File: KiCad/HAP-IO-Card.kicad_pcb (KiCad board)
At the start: 2 copper layers, 110 x 72 mm, 229 parts, among them CON601 AVR-JTAG-10, J201 TE_Connectivity_1-282834-0, J202 TE_Connectivity_282834-6, J203 GS3, J204 GS3, J205 GS3, J206 GS3, J207 GS3, J208 GS3, J209 GS3, J210 GS3, J211 TE_Connectivity_282834-6, J212 TE_Connectivity_1-282834-0, J401 TE_Connectivity_1-282834-0, J402 TE_Connectivity_282834-6, J501 TE_Connectivity_282834-3, J502 CONN_01X03_FEMALE, J601 ISP0, J602 ISP1, J603 CONN_01X02, J604 CONN_01X02, J605 CONN_01X02, J606 CONN_01X02, J607 CONN_01X03, J608 CONN_01X03, J701 5V_I/O_2, J702 5V_I/O_1, J703 NEO1, J704 NEO2, J705 NEO3, J706 NEO4, J707 CONN_01X03, Q201 ZXTN25050DFHTA, Q202 ZXTN25050DFHTA, Q203 ZXTN25050DFHTA, Q204 ZXTN25050DFHTA, Q205 ZXTN25050DFHTA, Q206 ZXTN25050DFHTA, Q207 ZXTN25050DFHTA, Q208 ZXTN25050DFHTA, U201 LTV-354T, U202 LTV-354T, U203 LTV-354T, U204 LTV-354T, U205 LTV-354T, U206 LTV-354T, U207 LTV-354T, U208 LTV-354T, U209 MCP23017, U401 ADS1115IDGST, U402 ADS1115IDGST, U501 LM1086-5V, U502 LM1086-3.3V, U701 TXB0102DCT

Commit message: More routing
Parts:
- CON601: footprint Pin_Headers:Pin_Header_Straight_2x06_Pitch2.54mm -> Pin_Headers:Pin_Header_Straight_2x05_Pitch2.54mm
- moved C409 6.62 mm to (118.2, 58.4), turned to 180 degrees
- moved U402 3.28 mm to (118.0, 52.7), turned to 90 degrees
- moved J203 2.16 mm to (128.3, 25.9)
- moved J204 2.16 mm to (124.7, 25.9)
- moved J205 2.16 mm to (121.1, 25.9)
- moved J206 2.16 mm to (117.4, 25.9)
- moved J207 2.16 mm to (113.5, 25.9)
- moved J208 2.16 mm to (109.9, 25.9)
- moved J209 2.16 mm to (106.3, 25.9)
- moved J210 2.16 mm to (102.7, 25.9)
- moved C506 1.20 mm to (66.8, 80.2)
- moved J601 1.11 mm to (60.8, 75.5)
- moved J602 1.11 mm to (56.7, 75.5)
- moved Q203 0.80 mm to (105.0, 37.9)
- moved C702 0.64 mm to (108.0, 59.6)
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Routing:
- net POWER3V3: track 73.6 -> 474.9 mm, vias 4 -> 12
- net SENSE_RDY_1: track 0.00 -> 116.0 mm
- net SENSE_SCL: track 0.00 -> 91.9 mm, vias 0 -> 2
- net DI7: track 0.00 -> 90.7 mm, vias 0 -> 4
- net DI8: track 0.00 -> 90.6 mm, vias 0 -> 5
- net 5V_I/O_1: track 6.31 -> 95.7 mm, vias 0 -> 6
- net SENSE_SDA: track 0.00 -> 88.5 mm, vias 0 -> 3
- net DI5: track 0.00 -> 85.6 mm, vias 0 -> 3
- net SENSE_RDY_2: track 0.00 -> 83.0 mm, vias 0 -> 7
- net 5V_I/O_Enable: track 0.00 -> 81.1 mm, vias 0 -> 4
- net DI6: track 0.00 -> 78.3 mm, vias 0 -> 5
- net POWER5V: track 283.7 -> 360.5 mm, vias 2 -> 8
- net Net-(JP302-Pad2): track 0.00 -> 76.1 mm
- net +12V: track 24.2 -> 97.9 mm
- net DI2: track 0.00 -> 73.2 mm, vias 0 -> 7
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- added copper zone on B.Cu, net Earth
- added copper zone on F.Cu, net Earth
- added copper zone on F.Cu, net POWER3V3
- added copper zone on F.Cu, net POWER5V

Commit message: Starting another routing pass
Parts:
- C209, C401, C402, C403, C404, C405, C406, C407, C408, C701, C704, D401, D402, D403, D404, D405, D406, D407, D408, D409, D410, D411, D412, D419, D420, D421, D422, R209, R210, R211, R212, R213, R214, R215, R216, R225, R226, R227, R228, R229, R230, R231, R232, R233, R235, R237, R239, R241, R243, R245, R247, R251, R252, R401, R402, R404, R405, R406, R407, R408, R409, R410, R411, R412, R413, R423, R424, R425, R426: moved to B.Cu
- U501, U502: footprint TO_SOT_Packages_THT:TO-220_Horizontal -> TO_SOT_Packages_THT:TO-220_Vertical
- moved J701 63.7 mm to (144.6, 27.6)
- moved J702 63.7 mm to (140.7, 27.6)
- moved J707 62.5 mm to (132.9, 20.2), turned to 90 degrees
- moved C701 60.6 mm to (145.7, 37.5), turned to 90 degrees
- moved C703 60.4 mm to (141.0, 37.5)
- moved J706 60.1 mm to (133.5, 24.2), turned to 90 degrees
- moved JP302 59.1 mm to (54.0, 85.6), turned to 180 degrees
- moved C704 58.7 mm to (141.8, 33.7)
- moved J705 56.3 mm to (133.5, 28.1), turned to 90 degrees
- moved U701 54.2 mm to (141.8, 34.7), turned to 0 degrees
- moved J704 52.8 mm to (133.4, 32.2), turned to 90 degrees
- moved JP301 52.6 mm to (47.8, 85.7), turned to 180 degrees
- moved J703 49.6 mm to (133.4, 36.3), turned to 90 degrees
- moved J608 48.7 mm to (87.8, 52.9), turned to 270 degrees
- moved R216 47.5 mm to (49.2, 38.7)
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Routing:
- net POWER3V3: track 474.9 -> 53.6 mm, vias 12 -> 1
- net POWER5V: track 360.5 -> 82.8 mm, vias 8 -> 0
- net SENSE_RDY_1: track 116.0 -> 0.00 mm
- net SENSE_SCL: track 91.9 -> 0.00 mm, vias 2 -> 0
- net 5V_I/O_1: track 95.7 -> 4.43 mm, vias 6 -> 1
- net DI7: track 90.7 -> 0.00 mm, vias 4 -> 0
- net DI8: track 90.6 -> 0.00 mm, vias 5 -> 0
- net SENSE_SDA: track 88.5 -> 0.00 mm, vias 3 -> 0
- net DI5: track 85.6 -> 0.00 mm, vias 3 -> 0
- net SENSE_RDY_2: track 83.0 -> 0.00 mm, vias 7 -> 0
- net 5V_I/O_Enable: track 81.1 -> 0.00 mm, vias 4 -> 0
- net DI6: track 78.3 -> 0.00 mm, vias 5 -> 0
- net Net-(JP302-Pad2): track 76.1 -> 0.00 mm
- net DI2: track 73.2 -> 0.00 mm, vias 7 -> 0
- net DI1: track 72.2 -> 0.00 mm, vias 5 -> 0
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- removed copper zone on F.Cu, net POWER3V3
- removed copper zone on F.Cu, net POWER5V
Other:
- outline, holes or cut-outs redrawn
- board text added: "Out"
- board text removed: "Common"

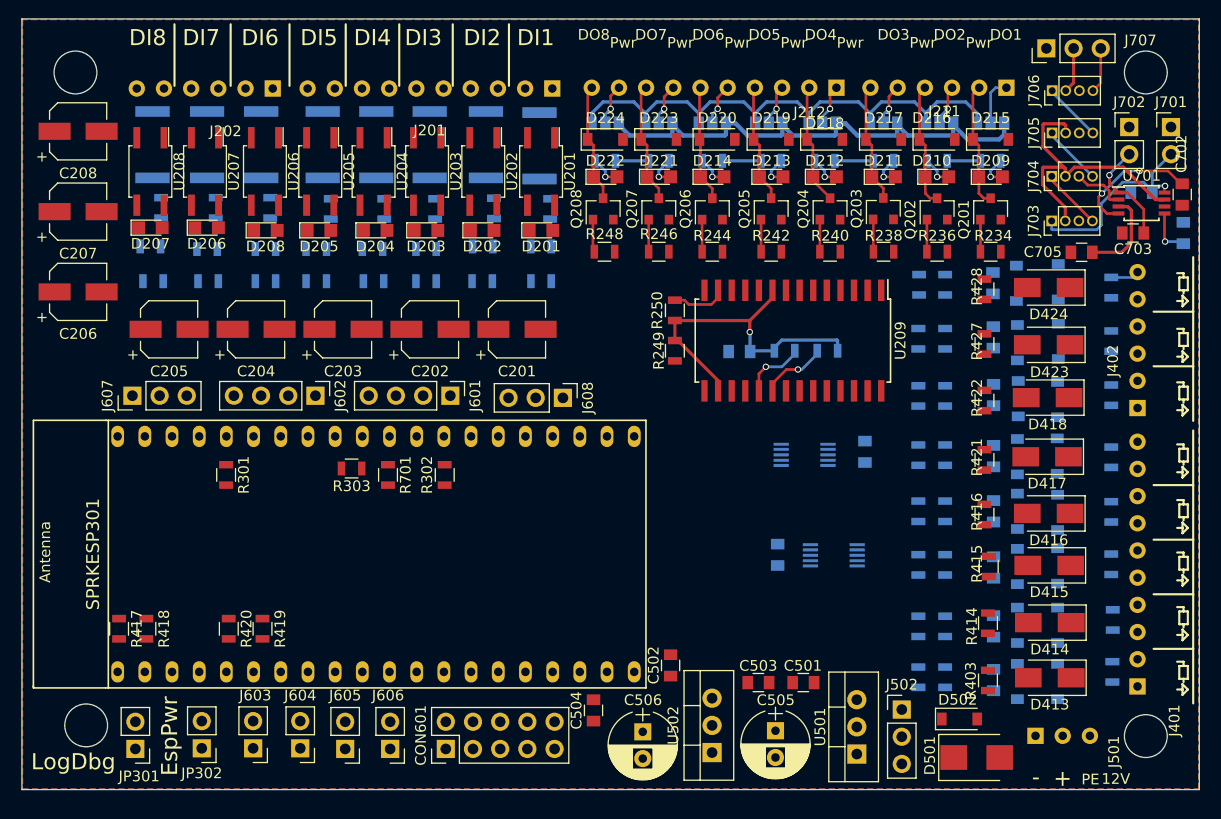
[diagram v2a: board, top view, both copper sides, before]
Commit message: Everything routed. ERC Ok
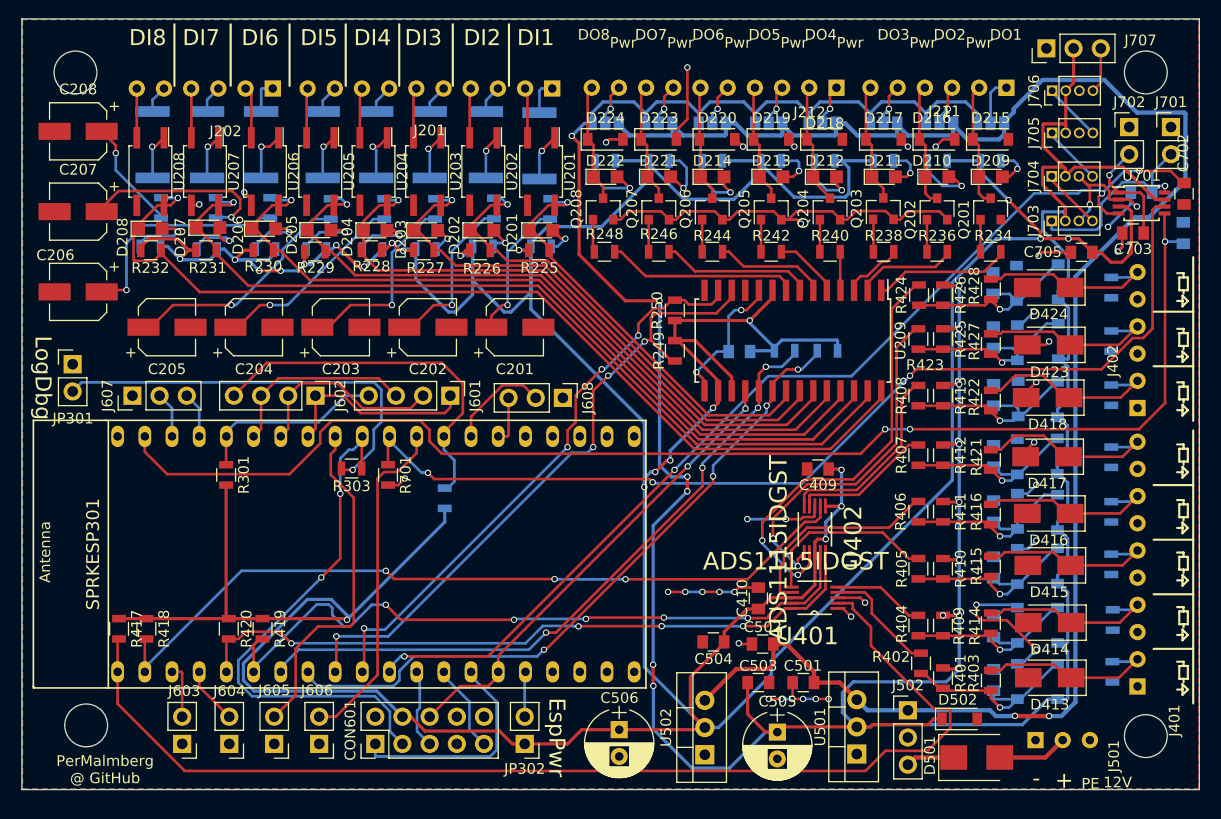
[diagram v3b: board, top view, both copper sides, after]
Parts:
- C409, C410, R225, R226, R227, R228, R229, R230, R231, R232, R401, R402, R404, R405, R406, R407, R408, R409, R410, R411, R412, R413, R423, R424, R425, R426, U401, U402: moved to F.Cu
- R302: moved to B.Cu
- moved JP301 36.4 mm to (42.0, 49.7), turned to 0 degrees
- moved JP302 30.2 mm to (84.2, 85.2)
- moved C504 12.9 mm to (101.8, 75.7), turned to 180 degrees
- moved D208 10.8 mm to (49.2, 37.1)
- moved C502 8.83 mm to (106.4, 75.9), turned to 180 degrees
- moved U402 7.03 mm to (111.3, 65.2), turned to 270 degrees
- moved J605 6.65 mm to (60.8, 85.2)
- moved J606 6.65 mm to (65.0, 85.2)
- moved J603 6.64 mm to (52.2, 85.2)
- moved J604 6.64 mm to (56.6, 85.2)
- moved CON601 6.61 mm to (70.2, 85.2)
- moved D207 5.40 mm to (54.6, 37.0)
- moved D206 5.35 mm to (59.8, 37.1)
- moved C409 4.68 mm to (111.6, 59.5), turned to 180 degrees
- moved C410 4.44 mm to (106.0, 71.6), turned to 90 degrees
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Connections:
- net 5V_I/O_1 renamed 5V_IO_1
- net 5V_I/O_2 renamed 5V_IO_2
- net 5V_I/O_Enable renamed 5V_IO_Enable
- net GPIO/1UART0_TX renamed GPIO1/UART0_TX
- SPRKESP301 pad 25: Net-(JP302-Pad2) -> Net-(SPRKESP301-Pad25)
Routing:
- net POWER3V3: track 53.6 -> 475.3 mm, vias 1 -> 23
- net POWER5V: track 82.8 -> 331.6 mm, vias 0 -> 15
- net Earth: track 5.04 -> 147.9 mm, vias 0 -> 41
- net +12V: track 47.6 -> 169.6 mm, vias 0 -> 2
- net 5V_IO_1: track 4.43 -> 124.1 mm, vias 1 -> 3
- net SENSE_RDY_1: track 0.00 -> 106.2 mm
- net 5V_IO_Enable: track 0.00 -> 94.4 mm, vias 0 -> 3
- net DI8: track 0.00 -> 90.5 mm, vias 0 -> 1
- net 5V_IO_2: track 12.3 -> 98.1 mm, vias 2 -> 4
- net DI7: track 0.00 -> 81.2 mm, vias 0 -> 1
- net SENSE_RDY_2: track 0.00 -> 74.2 mm, vias 0 -> 3
- net DI6: track 0.00 -> 73.9 mm, vias 0 -> 1
- net SENSE_SDA: track 0.00 -> 66.7 mm, vias 0 -> 5
- net DI5: track 0.00 -> 66.7 mm, vias 0 -> 1
- net SENSE_SCL: track 0.00 -> 65.2 mm, vias 0 -> 4
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
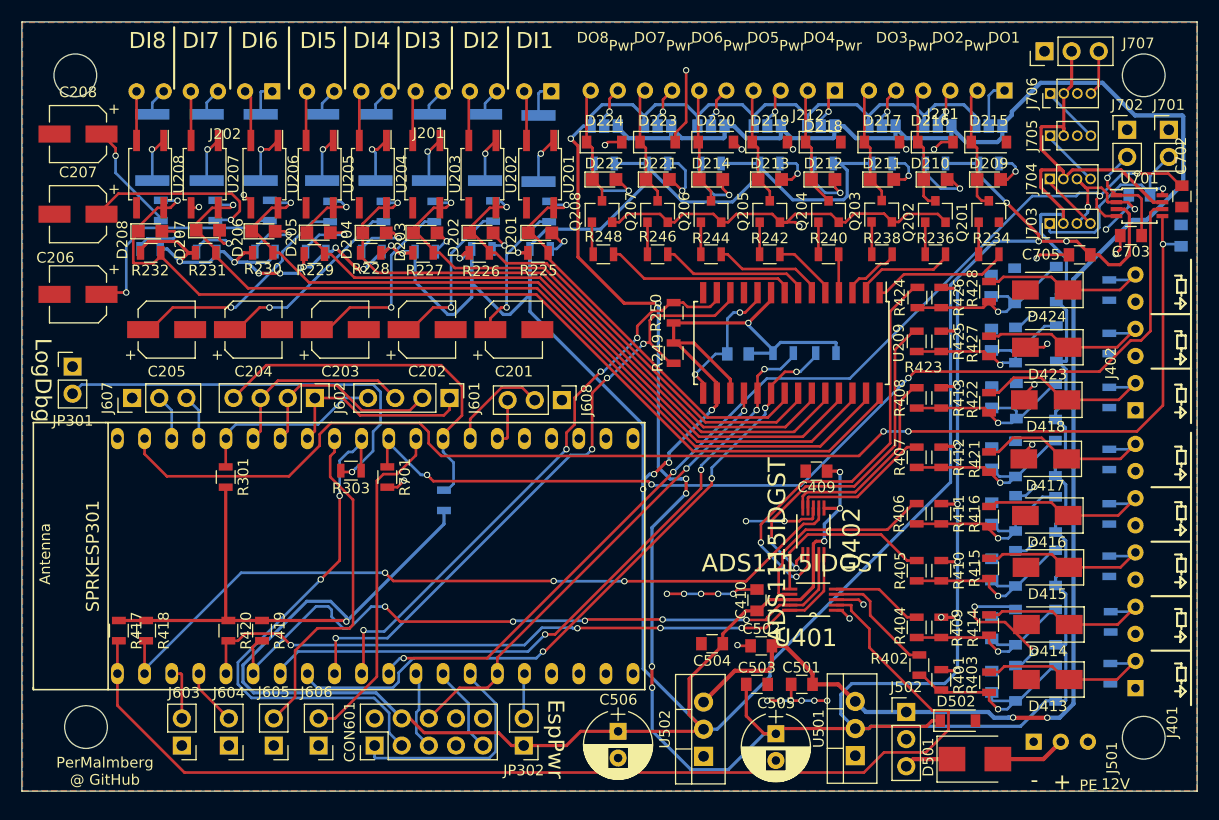
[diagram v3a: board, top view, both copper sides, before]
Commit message: Increased ground plane coverage
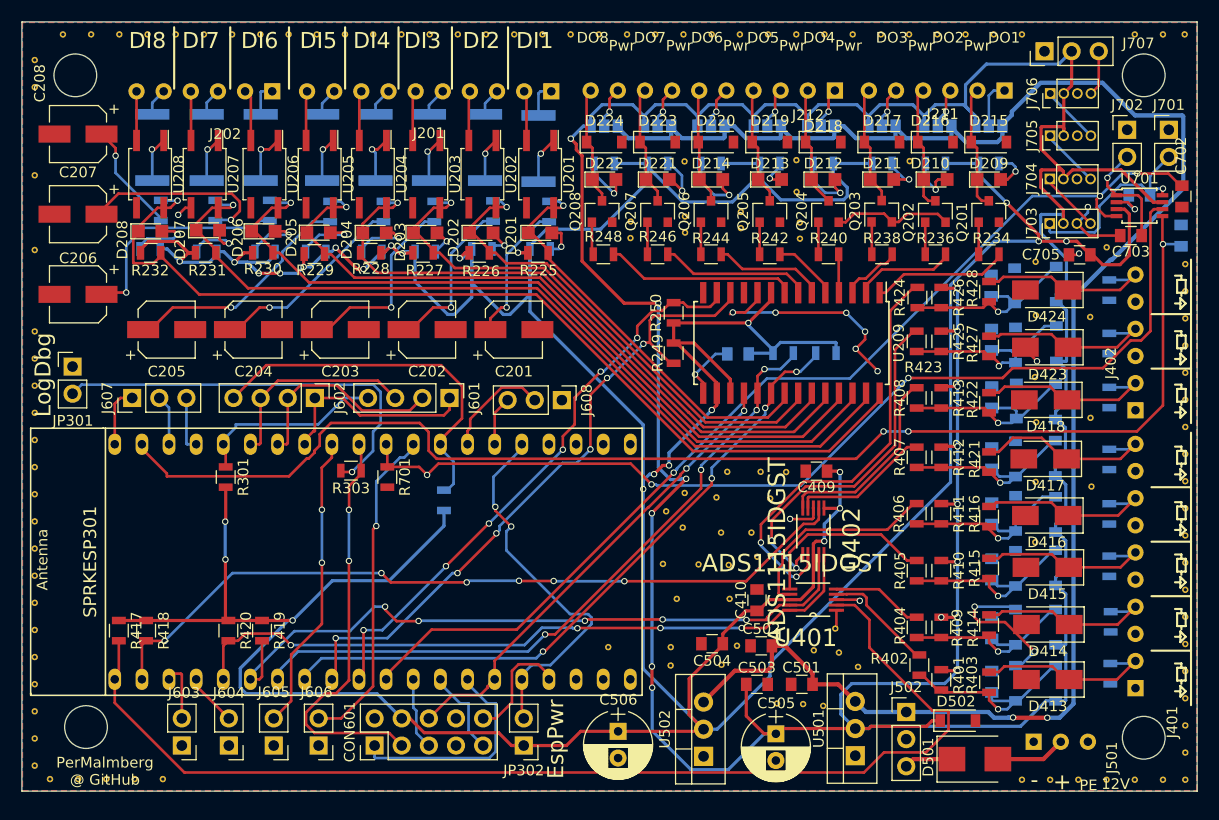
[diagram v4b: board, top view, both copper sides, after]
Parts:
- added REF**: StichingVia, StichingVIA:StichingVia, F.Cu at (132.1, 66.2)
- added REF**: StichingVia, StichingVIA:StichingVia, F.Cu at (120.3, 30.5)
- added REF**: StichingVia, StichingVIA:StichingVia, F.Cu at (99.2, 18.6)
- added REF**: StichingVia, StichingVIA:StichingVia, F.Cu at (96.5, 18.6)
- added REF**: StichingVia, StichingVIA:StichingVia, F.Cu at (93.9, 18.6)
- added REF**: StichingVia, StichingVIA:StichingVia, F.Cu at (91.2, 18.6)
- added REF**: StichingVia, StichingVIA:StichingVia, F.Cu at (88.6, 18.6)
- added REF**: StichingVia, StichingVIA:StichingVia, F.Cu at (86.0, 18.6)
- added REF**: StichingVia, StichingVIA:StichingVia, F.Cu at (83.3, 18.6)
- added REF**: StichingVia, StichingVIA:StichingVia, F.Cu at (80.7, 18.6)
- added REF**: StichingVia, StichingVIA:StichingVia, F.Cu at (78.0, 18.6)
- added REF**: StichingVia, StichingVIA:StichingVia, F.Cu at (75.4, 18.6)
- added REF**: StichingVia, StichingVIA:StichingVia, F.Cu at (104.2, 75.9)
- added REF**: StichingVia, StichingVIA:StichingVia, F.Cu at (72.8, 18.6)
- added REF**: StichingVia, StichingVIA:StichingVia, F.Cu at (70.1, 18.6)
- added REF**: StichingVia, StichingVIA:StichingVia, F.Cu at (67.5, 18.6)
- added REF**: StichingVia, StichingVIA:StichingVia, F.Cu at (64.8, 18.6)
- added REF**: StichingVia, StichingVIA:StichingVia, F.Cu at (62.2, 18.6)
- added REF**: StichingVia, StichingVIA:StichingVia, F.Cu at (59.5, 18.6)
- added REF**: StichingVia, StichingVIA:StichingVia, F.Cu at (56.9, 18.6)
- added REF**: StichingVia, StichingVIA:StichingVia, F.Cu at (54.3, 18.6)
- added REF**: StichingVia, StichingVIA:StichingVia, F.Cu at (51.6, 18.6)
- added REF**: StichingVia, StichingVIA:StichingVia, F.Cu at (49.0, 18.6)
- added REF**: StichingVia, StichingVIA:StichingVia, F.Cu at (102.7, 77.6)
- added REF**: StichingVia, StichingVIA:StichingVia, F.Cu at (46.4, 18.6)
- added REF**: StichingVia, StichingVIA:StichingVia, F.Cu at (43.7, 18.6)
- added REF**: StichingVia, StichingVIA:StichingVia, F.Cu at (41.1, 18.6)
- added REF**: StichingVia, StichingVIA:StichingVia, F.Cu at (38.4, 79.5)
- added REF**: StichingVia, StichingVIA:StichingVia, F.Cu at (38.4, 76.9)
- added REF**: StichingVia, StichingVIA:StichingVia, F.Cu at (38.4, 74.4)
- added REF**: StichingVia, StichingVIA:StichingVia, F.Cu at (38.4, 71.8)
- added REF**: StichingVia, StichingVIA:StichingVia, F.Cu at (38.4, 69.3)
- added REF**: StichingVia, StichingVIA:StichingVia, F.Cu at (38.4, 66.8)
- added REF**: StichingVia, StichingVIA:StichingVia, F.Cu at (38.4, 64.2)
- added REF**: StichingVia, StichingVIA:StichingVia, F.Cu at (107.9, 81.3)
- added REF**: StichingVia, StichingVIA:StichingVia, F.Cu at (38.4, 61.7)
- added REF**: StichingVia, StichingVIA:StichingVia, F.Cu at (38.4, 59.1)
- added REF**: StichingVia, StichingVIA:StichingVia, F.Cu at (38.4, 56.6)
- added REF**: StichingVia, StichingVIA:StichingVia, F.Cu at (38.4, 54.1)
- added REF**: StichingVia, StichingVIA:StichingVia, F.Cu at (38.4, 51.5)
- added REF**: StichingVia, StichingVIA:StichingVia, F.Cu at (38.4, 49.0)
- added REF**: StichingVia, StichingVIA:StichingVia, F.Cu at (38.4, 46.4)
- added REF**: StichingVia, StichingVIA:StichingVia, F.Cu at (38.4, 38.8)
- added REF**: StichingVia, StichingVIA:StichingVia, F.Cu at (38.4, 31.8)
- added REF**: StichingVia, StichingVIA:StichingVia, F.Cu at (38.4, 23.6)
- added REF**: StichingVia, StichingVIA:StichingVia, F.Cu at (110.3, 81.3)
- added REF**: StichingVia, StichingVIA:StichingVia, F.Cu at (38.4, 21.0)
- added REF**: StichingVia, StichingVIA:StichingVia, F.Cu at (112.2, 81.5)
- added REF**: StichingVia, StichingVIA:StichingVia, F.Cu at (113.7, 76.5)
- added REF**: StichingVia, StichingVIA:StichingVia, F.Cu at (115.5, 77.8)
- added REF**: StichingVia, StichingVIA:StichingVia, F.Cu at (113.4, 74.2)
- added REF**: StichingVia, StichingVIA:StichingVia, F.Cu at (111.3, 76.3)
- added REF**: StichingVia, StichingVIA:StichingVia, F.Cu at (132.1, 60.5)
- added REF**: StichingVia, StichingVIA:StichingVia, F.Cu at (132.1, 44.9)
- added REF**: StichingVia, StichingVIA:StichingVia, F.Cu at (132.1, 39.9)
- added REF**: StichingVia, StichingVIA:StichingVia, F.Cu at (104.5, 36.8)
- added REF**: StichingVia, StichingVIA:StichingVia, F.Cu at (104.5, 35.3)
- added REF**: StichingVia, StichingVIA:StichingVia, F.Cu at (94.2, 36.1)
- added REF**: StichingVia, StichingVIA:StichingVia, F.Cu at (94.2, 37.7)
- added REF**: StichingVia, StichingVIA:StichingVia, F.Cu at (99.3, 37.2)
- added REF**: StichingVia, StichingVIA:StichingVia, F.Cu at (99.3, 35.7)
- added REF**: StichingVia, StichingVIA:StichingVia, F.Cu at (108.8, 59.6)
- added REF**: StichingVia, StichingVIA:StichingVia, F.Cu at (106.4, 59.6)
- added REF**: StichingVia, StichingVIA:StichingVia, F.Cu at (132.2, 54.9)
- added REF**: StichingVia, StichingVIA:StichingVia, F.Cu at (103.2, 59.6)
- added REF**: StichingVia, StichingVIA:StichingVia, F.Cu at (99.3, 61.6)
- added REF**: StichingVia, StichingVIA:StichingVia, F.Cu at (97.5, 63.3)
- added REF**: StichingVia, StichingVIA:StichingVia, F.Cu at (102.7, 65.3)
- added REF**: StichingVia, StichingVIA:StichingVia, F.Cu at (100.6, 68.2)
- added REF**: StichingVia, StichingVIA:StichingVia, F.Cu at (99.1, 64.8)
- added REF**: StichingVia, StichingVIA:StichingVia, F.Cu at (103.4, 68.3)
- added REF**: StichingVia, StichingVIA:StichingVia, F.Cu at (106.0, 67.5)
- added REF**: StichingVia, StichingVIA:StichingVia, F.Cu at (105.5, 65.3)
- added REF**: StichingVia, StichingVIA:StichingVia, F.Cu at (107.3, 62.1)
- added REF**: StichingVia, StichingVIA:StichingVia, F.Cu at (132.1, 50.7)
- added REF**: StichingVia, StichingVIA:StichingVia, F.Cu at (102.2, 62.0)
- added REF**: StichingVia, StichingVIA:StichingVia, F.Cu at (98.5, 71.5)
- added REF**: StichingVia, StichingVIA:StichingVia, F.Cu at (92.1, 76.0)
- added REF**: StichingVia, StichingVIA:StichingVia, F.Cu at (103.5, 71.5)
- added REF**: StichingVia, StichingVIA:StichingVia, F.Cu at (98.0, 77.7)
- added REF**: StichingVia, StichingVIA:StichingVia, F.Cu at (98.0, 76.0)
- added REF**: StichingVia, StichingVIA:StichingVia, F.Cu at (97.2, 68.2)
- added REF**: StichingVia, StichingVIA:StichingVia, F.Cu at (109.7, 30.4)
- added REF**: StichingVia, StichingVIA:StichingVia, F.Cu at (109.7, 33.4)
- added REF**: StichingVia, StichingVIA:StichingVia, F.Cu at (110.0, 36.2)
- added REF**: StichingVia, StichingVIA:StichingVia, F.Cu at (137.3, 61.0)
- added REF**: StichingVia, StichingVIA:StichingVia, F.Cu at (110.0, 37.8)
- added REF**: StichingVia, StichingVIA:StichingVia, F.Cu at (144.0, 88.4)
- added REF**: StichingVia, StichingVIA:StichingVia, F.Cu at (141.4, 88.4)
- added REF**: StichingVia, StichingVIA:StichingVia, F.Cu at (138.8, 88.4)
- added REF**: StichingVia, StichingVIA:StichingVia, F.Cu at (136.1, 88.4)
- added REF**: StichingVia, StichingVIA:StichingVia, F.Cu at (133.5, 88.4)
- added REF**: StichingVia, StichingVIA:StichingVia, F.Cu at (130.8, 88.4)
- added REF**: StichingVia, StichingVIA:StichingVia, F.Cu at (146.1, 88.4)
- added REF**: StichingVia, StichingVIA:StichingVia, F.Cu at (146.1, 85.9)
- added REF**: StichingVia, StichingVIA:StichingVia, F.Cu at (146.1, 83.3)
- added REF**: StichingVia, StichingVIA:StichingVia, F.Cu at (137.2, 54.5)
- added REF**: StichingVia, StichingVIA:StichingVia, F.Cu at (146.1, 80.8)
- added REF**: StichingVia, StichingVIA:StichingVia, F.Cu at (146.1, 78.2)
- added REF**: StichingVia, StichingVIA:StichingVia, F.Cu at (146.1, 75.7)
- added REF**: StichingVia, StichingVIA:StichingVia, F.Cu at (146.1, 73.2)
- added REF**: StichingVia, StichingVIA:StichingVia, F.Cu at (146.1, 70.6)
- added REF**: StichingVia, StichingVIA:StichingVia, F.Cu at (146.1, 68.1)
- added REF**: StichingVia, StichingVIA:StichingVia, F.Cu at (146.1, 65.5)
- added REF**: StichingVia, StichingVIA:StichingVia, F.Cu at (146.1, 63.0)
- added REF**: StichingVia, StichingVIA:StichingVia, F.Cu at (146.1, 60.5)
- added REF**: StichingVia, StichingVIA:StichingVia, F.Cu at (146.1, 57.9)
- added REF**: StichingVia, StichingVIA:StichingVia, F.Cu at (137.2, 45.1)
- added REF**: StichingVia, StichingVIA:StichingVia, F.Cu at (146.1, 55.4)
- added REF**: StichingVia, StichingVIA:StichingVia, F.Cu at (146.1, 52.8)
- added REF**: StichingVia, StichingVIA:StichingVia, F.Cu at (146.1, 50.3)
- added REF**: StichingVia, StichingVIA:StichingVia, F.Cu at (146.1, 47.8)
- added REF**: StichingVia, StichingVIA:StichingVia, F.Cu at (146.1, 45.2)
- added REF**: StichingVia, StichingVIA:StichingVia, F.Cu at (146.1, 42.7)
- added REF**: StichingVia, StichingVIA:StichingVia, F.Cu at (146.1, 40.1)
- added REF**: StichingVia, StichingVIA:StichingVia, F.Cu at (50.4, 88.3)
- added REF**: StichingVia, StichingVIA:StichingVia, F.Cu at (47.8, 88.3)
- added REF**: StichingVia, StichingVIA:StichingVia, F.Cu at (45.1, 88.3)
- added REF**: StichingVia, StichingVIA:StichingVia, F.Cu at (138.8, 38.6)
- added REF**: StichingVia, StichingVIA:StichingVia, F.Cu at (42.5, 88.3)
- added REF**: StichingVia, StichingVIA:StichingVia, F.Cu at (39.9, 88.3)
- added REF**: StichingVia, StichingVIA:StichingVia, F.Cu at (38.4, 87.1)
- added REF**: StichingVia, StichingVIA:StichingVia, F.Cu at (38.4, 84.5)
- added REF**: StichingVia, StichingVIA:StichingVia, F.Cu at (38.4, 82.0)
- added REF**: StichingVia, StichingVIA:StichingVia, F.Cu at (146.1, 18.6)
- added REF**: StichingVia, StichingVIA:StichingVia, F.Cu at (144.0, 18.6)
- added REF**: StichingVia, StichingVIA:StichingVia, F.Cu at (141.4, 18.6)
- added REF**: StichingVia, StichingVIA:StichingVia, F.Cu at (130.8, 18.6)
- added REF**: StichingVia, StichingVIA:StichingVia, F.Cu at (128.2, 18.6)
- added REF**: StichingVia, StichingVIA:StichingVia, F.Cu at (99.2, 30.5)
- added REF**: StichingVia, StichingVIA:StichingVia, F.Cu at (125.5, 18.6)
- added REF**: StichingVia, StichingVIA:StichingVia, F.Cu at (122.9, 18.6)
- added REF**: StichingVia, StichingVIA:StichingVia, F.Cu at (120.3, 18.6)
- added REF**: StichingVia, StichingVIA:StichingVia, F.Cu at (117.6, 18.6)
- added REF**: StichingVia, StichingVIA:StichingVia, F.Cu at (115.0, 18.6)
- added REF**: StichingVia, StichingVIA:StichingVia, F.Cu at (112.3, 18.6)
- added REF**: StichingVia, StichingVIA:StichingVia, F.Cu at (109.7, 18.6)
- added REF**: StichingVia, StichingVIA:StichingVia, F.Cu at (107.1, 18.6)
- added REF**: StichingVia, StichingVIA:StichingVia, F.Cu at (104.4, 18.6)
- added REF**: StichingVia, StichingVIA:StichingVia, F.Cu at (101.8, 18.6)
- moved SPRKESP301 0.59 mm to (94.2, 79.1)
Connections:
- SPRKESP301 pad 25: Net-(SPRKESP301-Pad25) -> Net-(JP302-Pad2)
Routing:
- net Earth: track 147.9 -> 95.2 mm, vias 41 -> 16
- net Net-(JP302-Pad2): track 4.62 -> 35.7 mm, vias 0 -> 2
- net POWER5V: track 331.6 -> 346.2 mm
- net JTAG:MTDO: track 49.9 -> 38.8 mm
- net POWER3V3: track 475.3 -> 469.6 mm, vias 23 -> 25
- net GPIO5/LED: track 32.4 -> 27.9 mm, vias 0 -> 2
- net Net-(D222-Pad2): track 6.94 -> 4.95 mm
- net GPI39: track 5.75 -> 3.97 mm
- net Net-(D210-Pad2): track 6.30 -> 4.75 mm
- net DIGITAL_INTB: track 64.6 -> 63.0 mm
- net Net-(D213-Pad2): track 4.24 -> 2.93 mm
- net VSPI_D/MOSI: track 18.6 -> 19.8 mm
- net VSPI_Q/MISO: track 18.0 -> 19.2 mm
- net SENSE_SCL: track 65.2 -> 66.1 mm
- net GPIO3/UART0_RX: track 4.28 -> 5.20 mm
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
